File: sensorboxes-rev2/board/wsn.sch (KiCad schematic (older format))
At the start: 12 parts

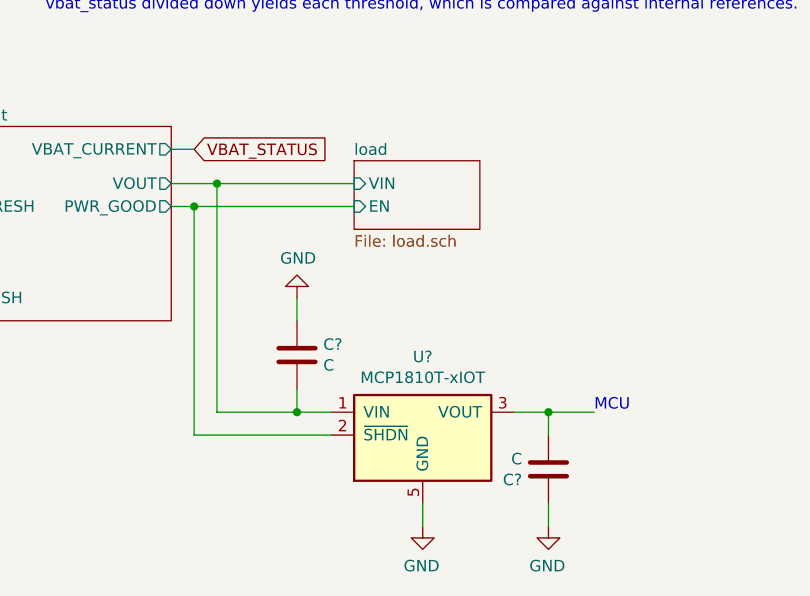
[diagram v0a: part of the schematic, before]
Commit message: added symbols for buck converter & boost converter + preliminary schematic for the overall system architecture.
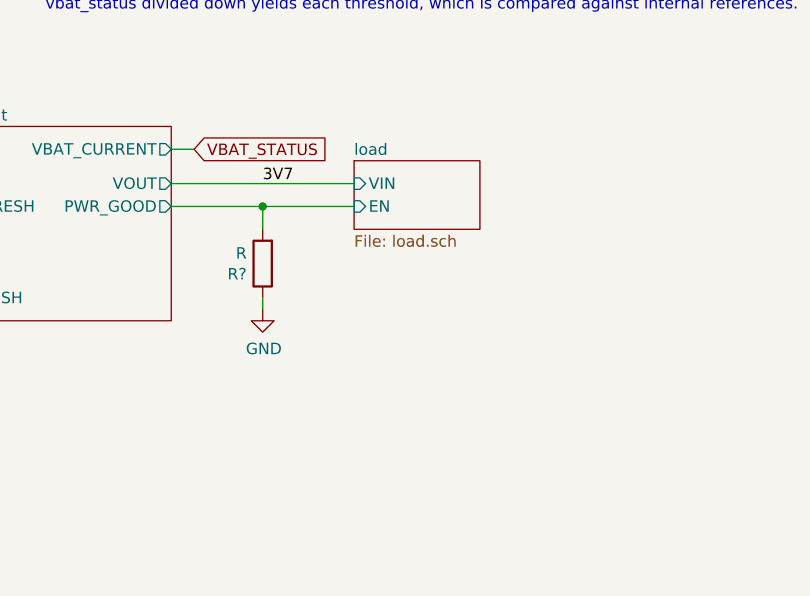
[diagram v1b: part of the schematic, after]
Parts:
- removed C? (x2): C, symbol Device:C
- removed U?: MCP1810T-xIOT, Package_TO_SOT_SMD:SOT-23-5, symbol wsn_sds_design_symbols:MCP1810T-xIOT
- added R?: R, symbol Device:R
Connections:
- net GND: now also R?.1
- net Power Management/PWR_GOOD: now also R?.2
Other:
- note removed: "MCU\n"
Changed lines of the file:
@@
 Text GLabel 3400 800  0    50   Input ~ 0
 VBAT_STATUS
-Text Notes 6700 4200 0    50   ~ 0
-MCU\n
-Connection ~ 5400 4200
-Wire Wire Line
-	5050 3200 5650 3200
-Connection ~ 5050 3200
-Wire Wire Line
-	5050 4200 5400 4200
-Wire Wire Line
-	5050 3200 5050 4200
-Wire Wire Line
-	4950 3300 5650 3300
-Connection ~ 4950 3300
-Wire Wire Line
-	4950 4300 5550 4300
-Wire Wire Line
-	4950 4300 4950 3300
-Connection ~ 6500 4200
-Wire Wire Line
-	6500 4200 6700 4200
-Wire Wire Line
-	6350 4200 6500 4200
-$Comp
-L Device:C C?
-U 1 1 5E779658
-P 6500 4450
-F 0 "C?" H 6615 4496 50  0000 L CNN
-F 1 "C" H 6615 4405 50  0000 L CNN
-F 2 "" H 6538 4300 50  0001 C CNN
-F 3 "~" H 6500 4450 50  0001 C CNN
-	1    6500 4450
-	-1   0    0    1
-$EndComp
-Wire Wire Line
-	6500 4200 6500 4300
-$Comp
-L power:GND #PWR?
-U 1 1 5E779651
-P 6500 4700
-F 0 "#PWR?" H 6500 4450 50  0001 C CNN
-F 1 "GND" H 6505 4527 50  0000 C CNN
-F 2 "" H 6500 4700 50  0001 C CNN
-F 3 "" H 6500 4700 50  0001 C CNN
-	1    6500 4700
-	-1   0    0    -1
-$EndComp
-Wire Wire Line
-	6500 4700 6500 4600
-$Comp
-L Device:C C?
-U 1 1 5E76B321
-P 5400 3950
-F 0 "C?" H 5515 3996 50  0000 L CNN
-F 1 "C" H 5515 3905 50  0000 L CNN
-F 2 "" H 5438 3800 50  0001 C CNN
-F 3 "~" H 5400 3950 50  0001 C CNN
-	1    5400 3950
-	1    0    0    -1
-$EndComp
-Wire Wire Line
-	5550 4200 5400 4200
-Wire Wire Line
-	5400 4200 5400 4100
-$Comp
-L power:GND #PWR?
-U 1 1 5E771201
-P 5400 3700
-F 0 "#PWR?" H 5400 3450 50  0001 C CNN
-F 1 "GND" H 5405 3527 50  0000 C CNN
-F 2 "" H 5400 3700 50  0001 C CNN
-F 3 "" H 5400 3700 50  0001 C CNN
-	1    5400 3700
-	1    0    0    1
-$EndComp
-Wire Wire Line
-	5400 3700 5400 3800
-Wire Wire Line
-	5950 4700 5950 4600
-$Comp
-L power:GND #PWR?
-U 1 1 5E769ACD
-P 5950 4700
-F 0 "#PWR?" H 5950 4450 50  0001 C CNN
-F 1 "GND" H 5955 4527 50  0000 C CNN
-F 2 "" H 5950 4700 50  0001 C CNN
-F 3 "" H 5950 4700 50  0001 C CNN
-	1    5950 4700
-	-1   0    0    -1
-$EndComp
-$Comp
-L wsn_sds_design_symbols:MCP1810T-xIOT U?
-U 1 1 5E767F71
-P 5950 4300
-F 0 "U?" H 5950 4642 50  0000 C CNN
-F 1 "MCP1810T-xIOT" H 5950 4551 50  0000 C CNN
-F 2 "Package_TO_SOT_SMD:SOT-23-5" H 5950 4650 50  0001 C CNN
-F 3 "" H 5950 4300 50  0001 C CNN
-	1    5950 4300
-	1    0    0    -1
-$EndComp
-Wire Wire Line
-	4850 3300 4950 3300
-Wire Wire Line
-	4850 3200 5050 3200
 Wire Wire Line
 	4850 3050 4950 3050
@@
 Wire Wire Line
 	3300 3700 3450 3700
+Wire Wire Line
+	4850 3200 5650 3200
+Wire Wire Line
+	4850 3300 5250 3300
+$Comp
+L Device:R R?
+U 1 1 5E5CC3C0
+P 5250 3550
+AR Path="/5E4C9109/5E5CC3C0" Ref="R?"  Part="1"
+AR Path="/5E5CC3C0" Ref="R?"  Part="1"
+F 0 "R?" H 5320 3596 50  0000 L CNN
+F 1 "R" H 5320 3505 50  0000 L CNN
+F 2 "" V 5180 3550 50  0001 C CNN
+F 3 "~" H 5250 3550 50  0001 C CNN
+	1    5250 3550
+	-1   0    0    1
+$EndComp
+$Comp
+L power:GND #PWR?
+U 1 1 5E5CC3C6
+P 5250 3750
+AR Path="/5E4C9109/5E5CC3C6" Ref="#PWR?"  Part="1"
+AR Path="/5E5CC3C6" Ref="#PWR?"  Part="1"
+F 0 "#PWR?" H 5250 3500 50  0001 C CNN
+F 1 "GND" H 5255 3577 50  0000 C CNN
+F 2 "" H 5250 3750 50  0001 C CNN
+F 3 "" H 5250 3750 50  0001 C CNN
+	1    5250 3750
+	1    0    0    -1
+$EndComp
+Wire Wire Line
+	5250 3750 5250 3700
+Wire Wire Line
+	5250 3400 5250 3300
+Connection ~ 5250 3300
+Wire Wire Line
+	5250 3300 5650 3300
+Text Label 5250 3200 0    50   ~ 0
+3V7
 $EndSCHEMATC

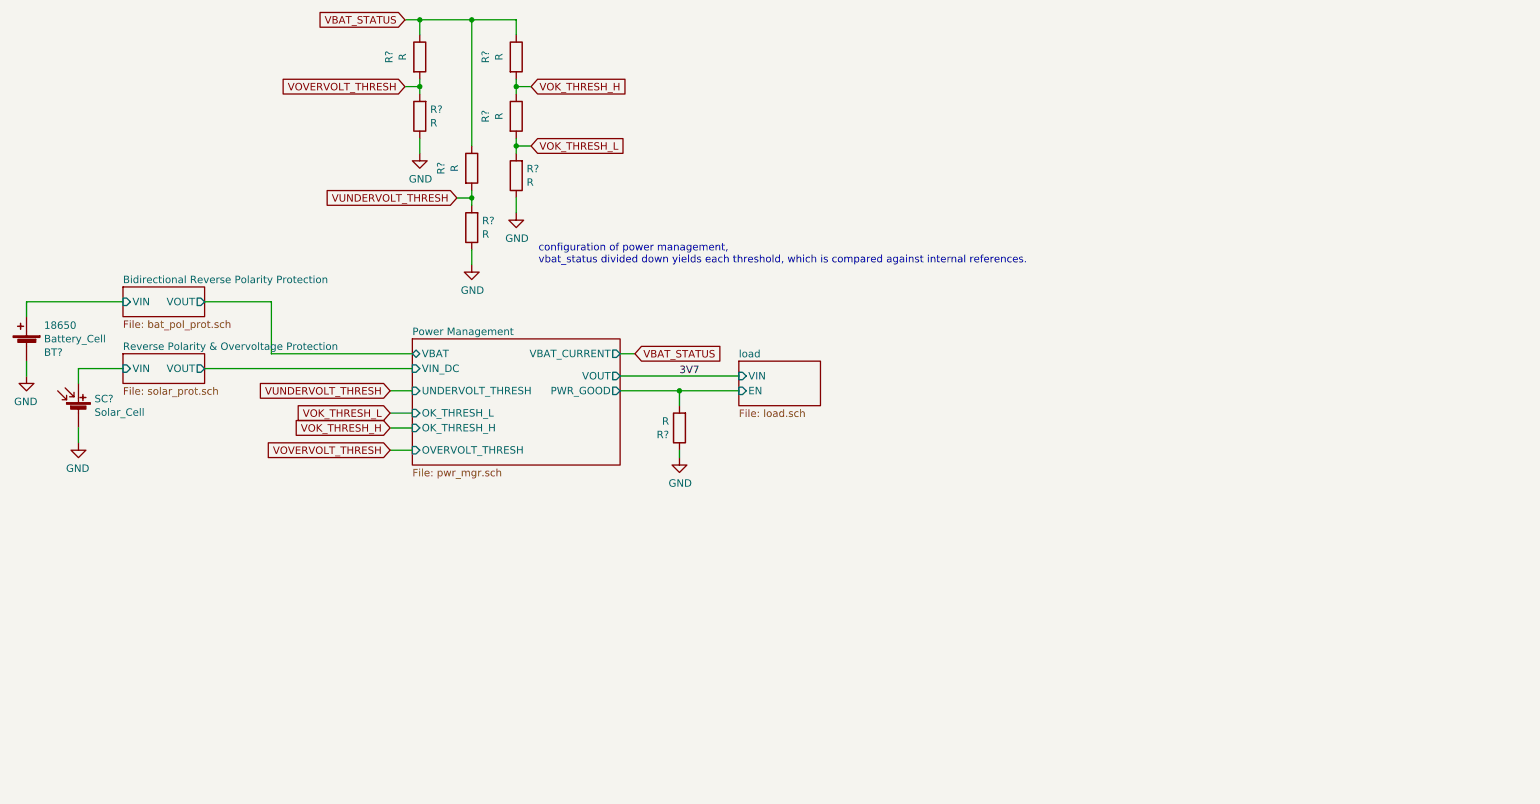
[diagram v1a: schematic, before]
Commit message: developed more of the schematic for the STM32 + radio. also picked out passives & figured out bidirectional battery polarity checking + reverse polarity protection for the solar panel.
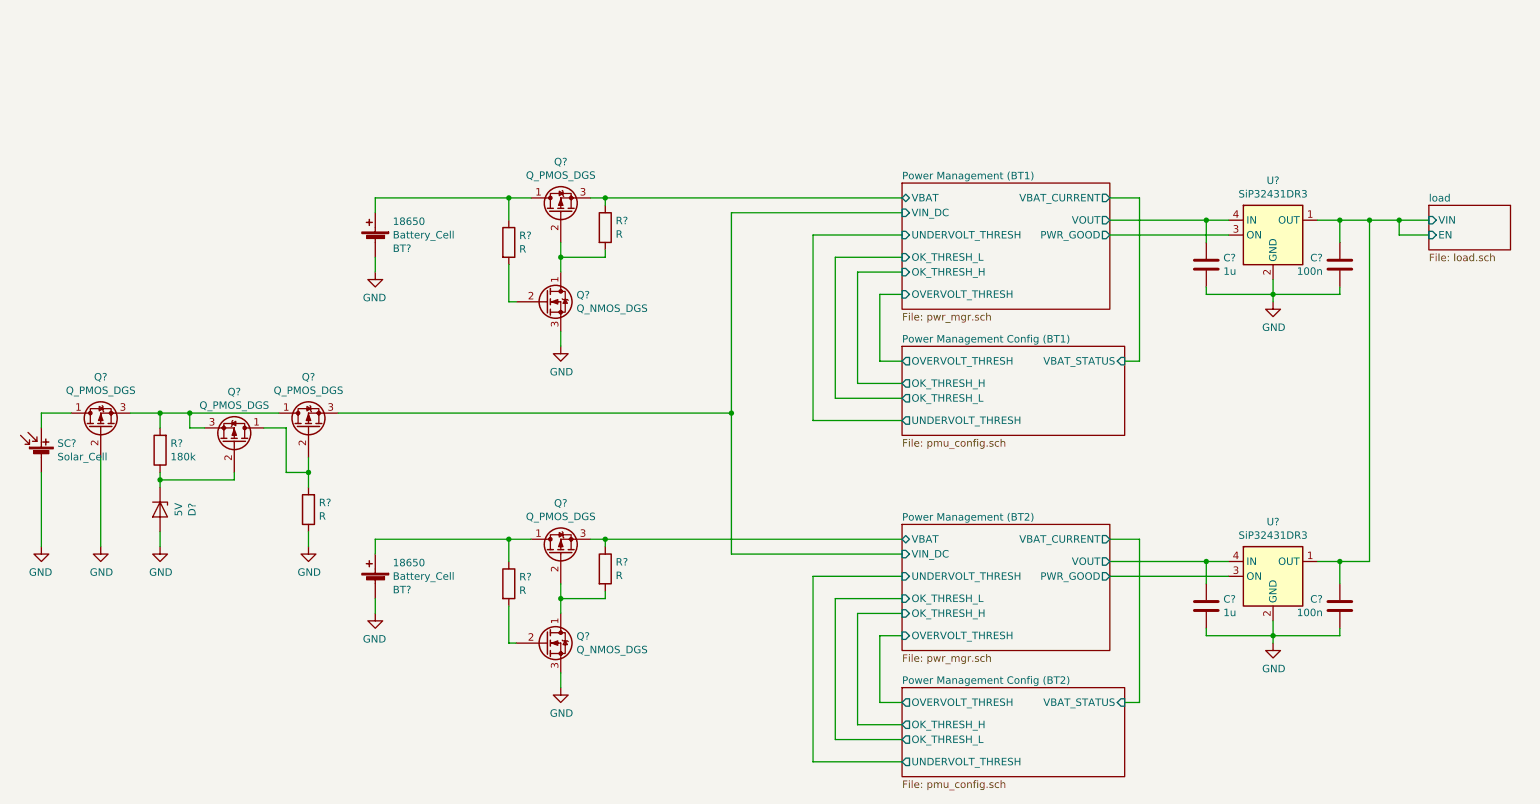
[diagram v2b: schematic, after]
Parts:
- removed R? (x8): R, symbol Device:R
- added BT?: Battery_Cell, symbol Device:Battery_Cell
- added C? (x2): 1u, symbol Device:C
- added C? (x2): 100n, symbol Device:C
- added D?: 5V, symbol Device:D_Zener
- added Q? (x2): Q_NMOS_DGS, symbol Device:Q_NMOS_DGS
- added Q? (x5): Q_PMOS_DGS, symbol Device:Q_PMOS_DGS
- added R? (x5): R, symbol Device:R
- added R?: 180k, symbol Device:R
- added U? (x2): SiP32431DR3, Package_TO_SOT_SMD:SOT-363_SC-70-6, symbol wsn_sds_design_symbols:SiP32431DR3
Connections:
- net GND: now also BT?.2 (-), C?.2, C?.2, C?.2, C?.2, D?.2 (A), Q?.2 (G), Q?.3 (S), Q?.3 (S), R?.1, U?.2 (GND), U?.2 (GND), U?.5 (GND), U?.5 (GND)
- net Bidirectional Reverse Polarity Protection/VIN: no longer names the net of BT?.1 (+)
- net Bidirectional Reverse Polarity Protection/VIN: now also Q?.1 (D), R?.1
- net Reverse Polarity & Overvoltage Protection/VIN: no longer names the net of SC?.1 (+)
- net Reverse Polarity & Overvoltage Protection/VIN: now also Q?.1 (D)
- new net: BT?.1 (+), Q?.1 (D), R?.1
- new net: Q?.2 (G), R?.2 (x2)
- new net: Q?.1 (D), Q?.2 (G), R?.2 (x3)
- new net: Q?.1 (D), Q?.3 (S), Q?.3 (S), R?.2
- new net: D?.1 (K), Q?.2 (G), R?.1
- new net Power Management (BT1)/PWR_GOOD: U?.3 (ON)
- new net Power Management (BT1)/VBAT: Q?.3 (S), R?.1
- new net Power Management (BT1)/VIN_DC: Q?.3 (S)
- new net Power Management (BT1)/VOUT: C?.1, U?.4 (IN)
- new net Power Management (BT2)/PWR_GOOD: U?.3 (ON)
- new net Power Management (BT2)/VBAT: Q?.3 (S), R?.1
- new net Power Management (BT2)/VOUT: C?.1, U?.4 (IN)
- new net load/EN: C?.1, C?.1, U?.1 (OUT), U?.1 (OUT)
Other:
- note removed: "configuration of power management,\nvbat_status divided down yields each threshold, which is compared against internal references."
- moved on the sheet: BT?, SC?

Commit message: some preliminary power figure estimation
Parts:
- removed Q?: Q_PMOS_DGS, symbol Device:Q_PMOS_DGS
- removed R?: R, symbol Device:R
- added D? (x2): 5V, symbol Device:D_Zener
- added JP? (x2): SolderJumper_2_Bridged, symbol Jumper:SolderJumper_2_Bridged
- added JP?: SolderJumper_2_Open, symbol Jumper:SolderJumper_2_Open
- added Q?: Q_PMOS_DGS, symbol Device:Q_PMOS_DGS
- added R? (x3): 470k, symbol Device:R
- R? (x2): value R -> 10M
- R?: value 180k -> 120k
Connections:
- wire segments 117 -> 135
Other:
- note added: "LT1389, DMG3401LSN-7"
- note added: "absolute worst case charging loss: 5 uA max, typ. 2 uA if polarity protection is skipped checked\n\n1.5 uA of which doesn't exist if no solar panel attached\n\nbattery leakage should be 0.5 uA + typ sleep power of control units (1.2 uA + 1.28 uA if no standby, else 1.5 uA total on standby w/ RTC)"
- note added: "alternative to this: SiP32101"
- note added: "assuming leakage doesn't flip the transistors on, average current consumption should be 400 nA max"
- note added: "average loss from panel within voltage limits = 1.5 uA?"
- note added: "need <8V gate-source zener clamp to prevent mosfet destruction\n\nmin zener current for stabilization * Resistor + Vzener = threshold?"
- note added: "reverse polarity clamp should activate at 5.5V, overvoltage protection should activate at 5.1V"
- note added: "solder jumpers to forgo the polarity checking for efficiency"
- note added: "worst case 1 uA"
- note added: "worst case 4V applied across resistors totaling to 10M -> 400 nA + approx 400 nA from charger.\n\nworst case 1 uA"
- moved on the sheet: D?, Q?, R?, SC?

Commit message: dont know if i committed everything
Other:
- note added: "absolute worst case charging loss: 5 uA max, typ. 2.5 uA if polarity protection is skipped checked\n\nbattery leakage should be 0.5 uA + typ sleep power of control units (1.2 uA + 1.28 uA if no standby, else 1.5 uA total on standby w/ RTC)"
- note removed: "absolute worst case charging loss: 5 uA max, typ. 2 uA if polarity protection is skipped checked\n\n1.5 uA of which doesn't exist if no solar panel attached\n\nbattery leakage should be 0.5 uA + typ sleep power of control units (1.2 uA + 1.28 uA if no standby, else 1.5 uA total on standby w/ RTC)"
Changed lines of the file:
@@
 worst case 1 uA
 Text Notes 8550 5700 0    50   ~ 0
-absolute worst case charging loss: 5 uA max, typ. 2 uA if polarity protection is skipped checked\n\n1.5 uA of which doesn't exist if no solar panel attached\n\nbattery leakage should be 0.5 uA + typ sleep power of control units (1.2 uA + 1.28 uA if no standby, else 1.5 uA total on standby w/ RTC)
+absolute worst case charging loss: 5 uA max, typ. 2.5 uA if polarity protection is skipped checked\n\nbattery leakage should be 0.5 uA + typ sleep power of control units (1.2 uA + 1.28 uA if no standby, else 1.5 uA total on standby w/ RTC)
 $Comp
 L Jumper:SolderJumper_2_Bridged JP?
